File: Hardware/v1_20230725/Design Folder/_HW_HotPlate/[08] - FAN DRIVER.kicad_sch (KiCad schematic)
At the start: 6 parts, among them J903 RCPT_2POS_2.54MM_VERT, Q801 AS3400

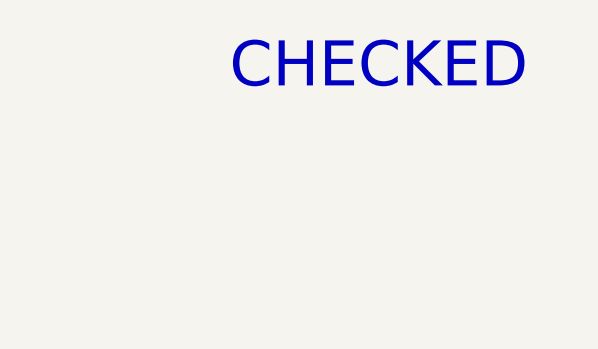
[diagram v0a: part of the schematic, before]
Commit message: Schematic library has been updated
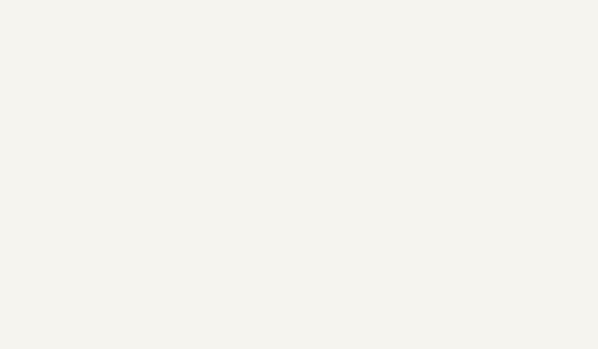
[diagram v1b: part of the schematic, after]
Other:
- note removed: "CHECKED"
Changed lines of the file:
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@@
 (kicad_sch (version 20230121) (generator eeschema)
-  (paper "B")
+  (paper "C")
   (title_block
     (title "Hot Plate")
@@
     (company "Mend0z0")
     (comment 1 "v1")
+    (comment 2 "RELEASED")
     (comment 3 "Siavash Taher Parvar")
     (comment 8 "N/A")
@@
     (stroke (width 0) (type default))
   )
-  (text "CHECKED" (at 381 35.56 0)
-    (effects (font (size 5 5)) (justify left bottom))
-  )
   (text "330uA @ +3v3DC" (at 129.54 160.02 0)

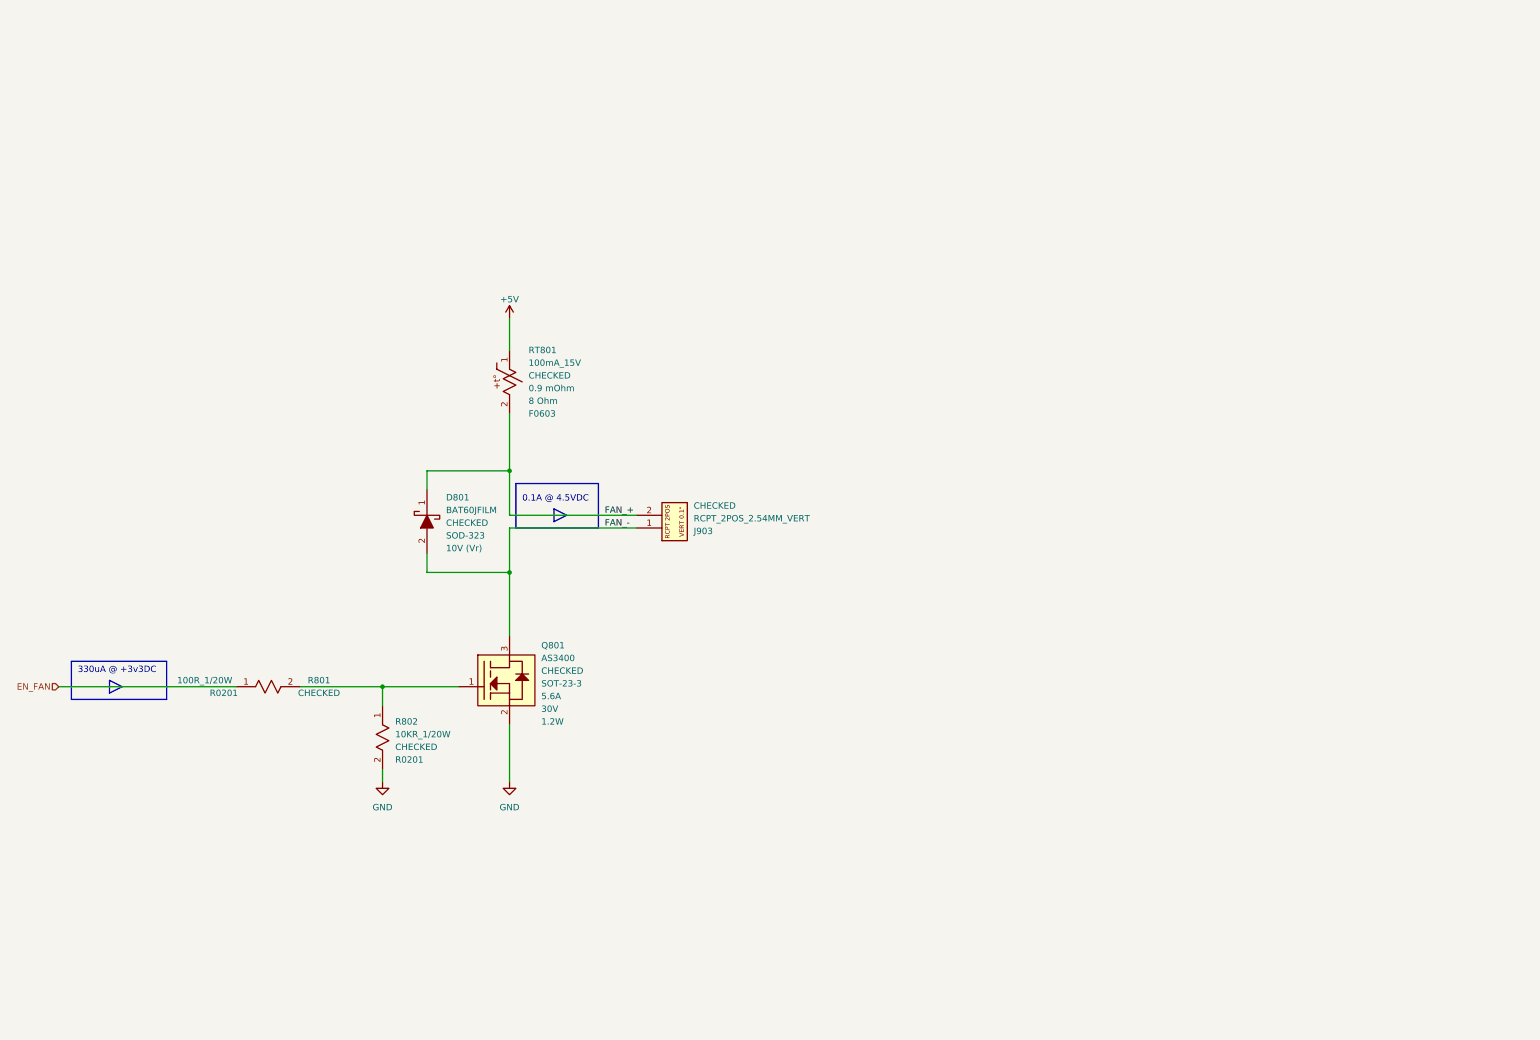
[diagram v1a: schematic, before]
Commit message: components have been updated
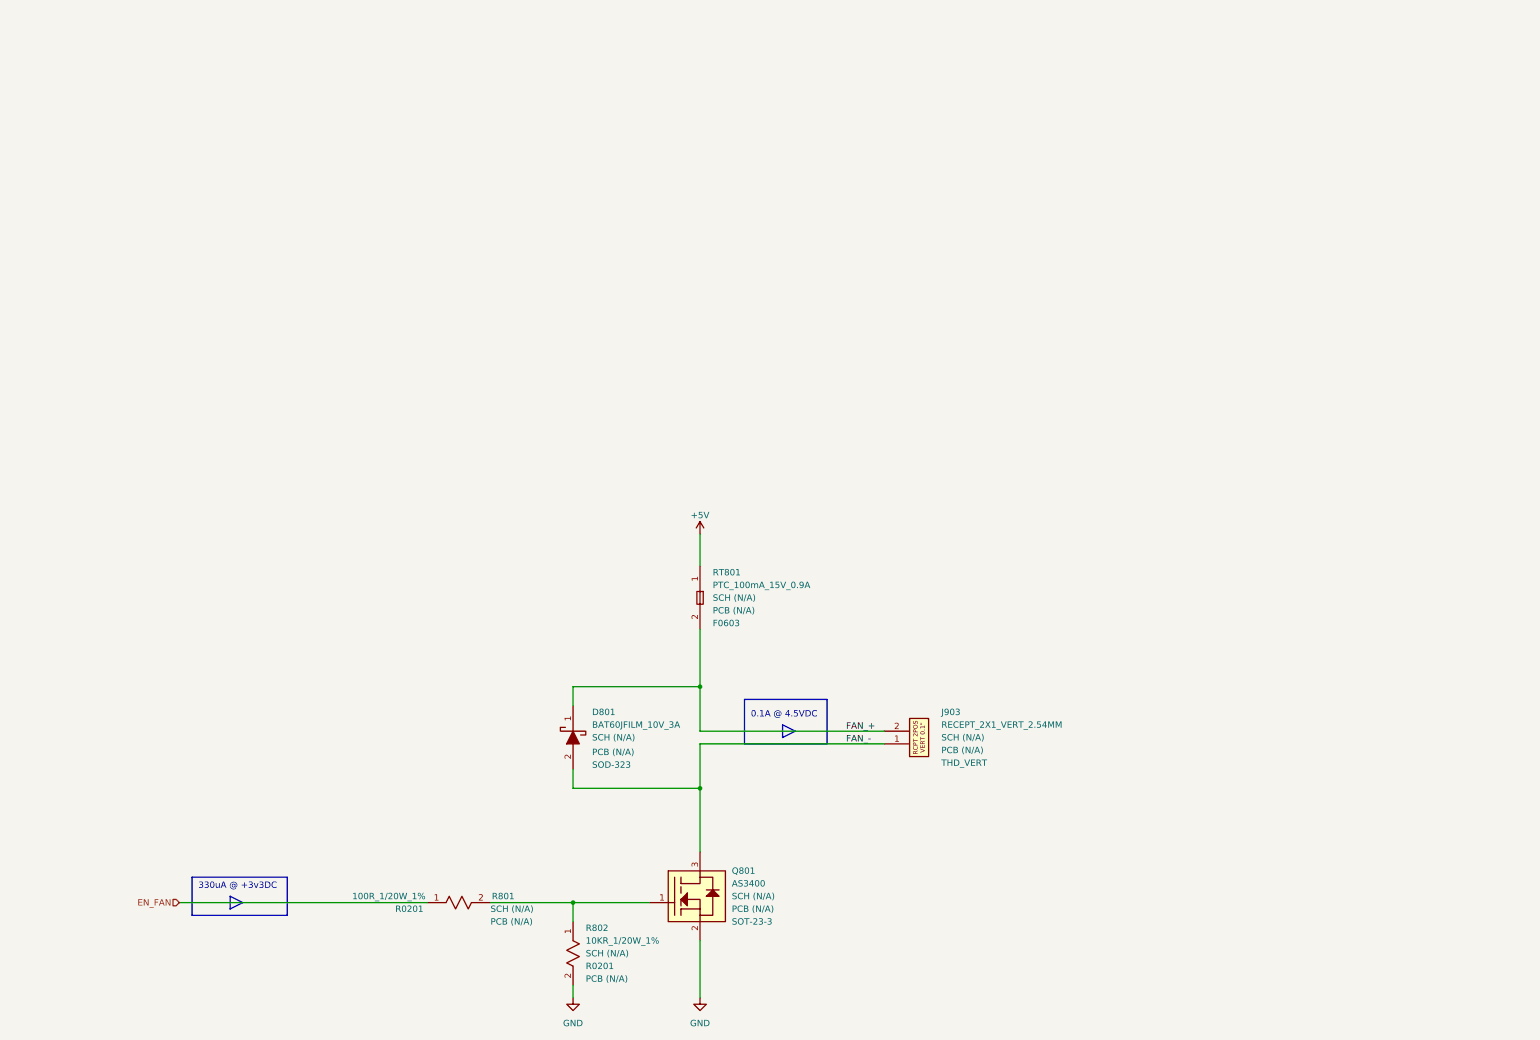
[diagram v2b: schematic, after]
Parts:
- D801: value BAT60JFILM -> BAT60JFILM_10V_3A; symbol _SCHLIB_HotPlate:SCHOTTKY_BAT60JFILM_SOD-323 -> _SCHLIB_HotPlate:DIODE_SCHOTTKY_BAT60JFILM_10V_3A_SOD-323; Manufacturer (none) -> STMicroelectronics; PCB CHECk (none) -> PCB (N/A); Part Number BAT60JFILM -> (none); Part Number (Manufacturer) (none) -> BAT60JFILM; Part Number (Vendor) (none) -> 497-3707-2-ND; SCH CHECK CHECKED -> SCH (N/A); Vendor (none) -> Digikey; Vr 10V (Vr) -> (none)
- J903: value RCPT_2POS_2.54MM_VERT -> RECEPT_2X1_VERT_2.54MM; symbol _SCHLIB_HotPlate:CONN_RCPT_2POS_2.54MM_VERT -> _SCHLIB_HotPlate:CONN_RECEPT_2POS_VERT_2.54MM; Manufacturer (none) -> Adam Tech; PCB CHECk (none) -> PCB (N/A); Package (none) -> THD_VERT; Part Number RS1-02-G -> (none); Part Number (Manufacturer) (none) -> RS1-02-G; Part Number (Vendor) (none) -> 2057-RS1-02-G-ND; SCH CHECK CHECKED -> SCH (N/A); Vendor (none) -> Digikey
- Q801: symbol _SCHLIB_HotPlate:Q_AS3400 -> _SCHLIB_HotPlate:Q_MOSFET_AS3400_N-CH_30V_5.6A_1.2W_SOT-23-3; Manufacturer (none) -> ANBON SEMICONDUCTOR (INT'L) LIMITED; Max Current 5.6A -> (none); Max P 1.2W -> (none); Max Vds 30V -> (none); PCB CHECk (none) -> PCB (N/A); Part Number AS3400 -> (none); Part Number (Manufacturer) (none) -> AS3400; Part Number (Vendor) (none) -> 4530-AS3400TR-ND; SCH CHECK CHECKED -> SCH (N/A); Vendor (none) -> Digikey
- R801: value 100R_1/20W -> 100R_1/20W_1%; symbol _SCHLIB_HotPlate:RES_100R_1/20W-R0201 -> _SCHLIB_HotPlate:RES_100R_1/20W_1%_R0201; Manufacturer (none) -> Stackpole Electronics Inc; PCB CHECk (none) -> PCB (N/A); Part Number RMCF0201FT100R -> (none); Part Number (Manufacturer) (none) -> RMCF0201FT100R; Part Number (Vendor) (none) -> RMCF0201FT100RTR-ND; SCH CHECK CHECKED -> SCH (N/A); Vendor (none) -> Digikey
- R802: value 10KR_1/20W -> 10KR_1/20W_1%; symbol _SCHLIB_HotPlate:RES_10KR_1/20W-R0201 -> _SCHLIB_HotPlate:RES_10KR_1/20W_1%_R0201; Manufacturer (none) -> Stackpole Electronics Inc; PCB CHECk (none) -> PCB (N/A); Part Number RMCF0201FT10K0 -> (none); Part Number (Manufacturer) (none) -> RMCF0201FT10K0; Part Number (Vendor) (none) -> RMCF0201FT10K0TR-ND; SCH CHECK CHECKED -> SCH (N/A); Vendor (none) -> Digikey
- RT801: value 100mA_15V -> PTC_100mA_15V_0.9A; symbol _SCHLIB_HotPlate:PTC_0ZCM0010FF2G_F0603 -> _SCHLIB_HotPlate:FUSE_PTC_0ZCM0010FF2G_0.1A_0.25A_15V_0.9A_F0603; Init resistance 0.9 mOhm -> (none); Manufacturer (none) -> Bel Fuse Inc.; PCB CHECk (none) -> PCB (N/A); Part Number 0ZCM0010FF2G -> (none); Part Number (Manufacturer) (none) -> 0ZCM0010FF2G; Part Number (Vendor) (none) -> 507-1818-2-ND; Post trip resistance 8 Ohm -> (none); SCH CHECK CHECKED -> SCH (N/A); Vendor (none) -> Digikey
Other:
- moved on the sheet: D801, J903, Q801, R801, R802

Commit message: Updating hardware format structure
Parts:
- Q801: footprint Package_TO_SOT_SMD:SOT-23-3 -> Package_TO_SOT_SMD:SOT-23
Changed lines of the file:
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@@
       (effects (font (size 1.27 1.27)) (justify left))
     )
-    (property "Footprint" "Package_TO_SOT_SMD:SOT-23-3" (at 246.38 176.53 0)
+    (property "Footprint" "Package_TO_SOT_SMD:SOT-23" (at 246.38 176.53 0)
       (effects (font (size 1.27 1.27)) (justify left) hide)
     )
